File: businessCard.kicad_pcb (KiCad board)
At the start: 2 copper layers, 88.6 x 50.6 mm, 24 parts

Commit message: Perf board bottom right
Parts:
- removed the 0402 at (131.5, 55.0)
- removed the 0402 at (127.0, 49.0)
- removed the 0402 at (127.0, 55.0)
- removed the 0402 at (127.0, 52.0)
- removed the 0402 at (131.5, 52.0)
- removed the 0402 at (131.5, 49.0)
- removed the 0603 at (119.2, 58.5)
- removed the 0603 at (123.7, 65.5)
- removed the 0603 at (119.2, 65.5)
- removed the 0603 at (119.2, 62.0)
- removed the 0603 at (123.7, 62.0)
- removed the 0603 at (123.7, 58.5)
- added 0402: R_0402_1005Metric, Resistor_SMD:R_0402_1005Metric, B.Cu at (113.2, 44.0)
- added 0402: R_0402_1005Metric, Resistor_SMD:R_0402_1005Metric, B.Cu at (113.2, 50.0)
- added 0402: R_0402_1005Metric, Resistor_SMD:R_0402_1005Metric, B.Cu at (113.2, 47.0)
- added 0402: R_0402_1005Metric, Resistor_SMD:R_0402_1005Metric, B.Cu at (117.8, 47.0)
- added 0402: R_0402_1005Metric, Resistor_SMD:R_0402_1005Metric, B.Cu at (117.8, 50.0)
- added 0402: R_0402_1005Metric, Resistor_SMD:R_0402_1005Metric, B.Cu at (117.8, 44.0)
- added 0603: R_0603_1608Metric, Resistor_SMD:R_0603_1608Metric, B.Cu at (108.8, 45.0)
- added 0603: R_0603_1608Metric, Resistor_SMD:R_0603_1608Metric, B.Cu at (108.8, 52.0)
- added 0603: R_0603_1608Metric, Resistor_SMD:R_0603_1608Metric, B.Cu at (104.2, 45.0)
- added 0603: R_0603_1608Metric, Resistor_SMD:R_0603_1608Metric, B.Cu at (108.8, 48.5)
- added 0603: R_0603_1608Metric, Resistor_SMD:R_0603_1608Metric, B.Cu at (104.2, 52.0)
- added 0603: R_0603_1608Metric, Resistor_SMD:R_0603_1608Metric, B.Cu at (104.2, 48.5)
- added G***: LOGO, LOGO, B.Cu at (174.0, 57.5)
- added QFN-48-7x7mm: QFN-48-1EP_7x7mm_P0.5mm_EP3.5x3.5mm, Package_DFN_QFN:QFN-48-1EP_7x7mm_P0.5mm_EP3.5x3.5mm, B.Cu at (127.0, 72.8)
- added REF**: Perf_Board, Connector_PinHeader_2.54mm:Perf_Board, F.Cu at (184.9, 74.9)
- added Ruler: Metric_Ruler_90mm, Ruler:Metric_Ruler_98mm, B.Cu at (178.5, 86.5)
- added SOT-223: SOT-223, Package_TO_SOT_SMD:SOT-223, B.Cu at (138.5, 50.5)
- added SOT-23: SOT-23, Package_TO_SOT_SMD:SOT-23, B.Cu at (138.4, 44.5)
- added TQFP-32-7x7mm: TQFP-32_7x7mm_P0.8mm, Package_QFP:TQFP-32_7x7mm_P0.8mm, B.Cu at (127.0, 48.0)
- added TQFP-48-7x7mm: TQFP-48_7x7mm_P0.5mm, Package_QFP:TQFP-48_7x7mm_P0.5mm, B.Cu at (127.0, 61.2)
- moved 0201 15.0 mm to (104.3, 61.0)
- moved 0201 15.0 mm to (104.3, 55.0)
- moved 0201 15.0 mm to (108.8, 58.0)
- moved 0201 15.0 mm to (108.8, 55.0)
- moved 0201 15.0 mm to (108.9, 61.0)
- moved 0201 15.0 mm to (104.3, 58.0)
- moved 0805 3.96 mm to (113.2, 57.5)
- moved 0805 3.96 mm to (117.7, 53.5)
- moved 0805 3.96 mm to (117.7, 61.5)
- moved 0805 3.96 mm to (117.7, 57.5)
- moved 0805 3.96 mm to (113.2, 53.5)
- moved 0805 3.96 mm to (113.2, 61.5)
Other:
- board text added: "Linktree: linktr.ee/charlienicholson GitHub: github.com/crnicholson"
- board text added: "Mini perf board"
- board text added: "Scan for website:"
- board text added: "mm"

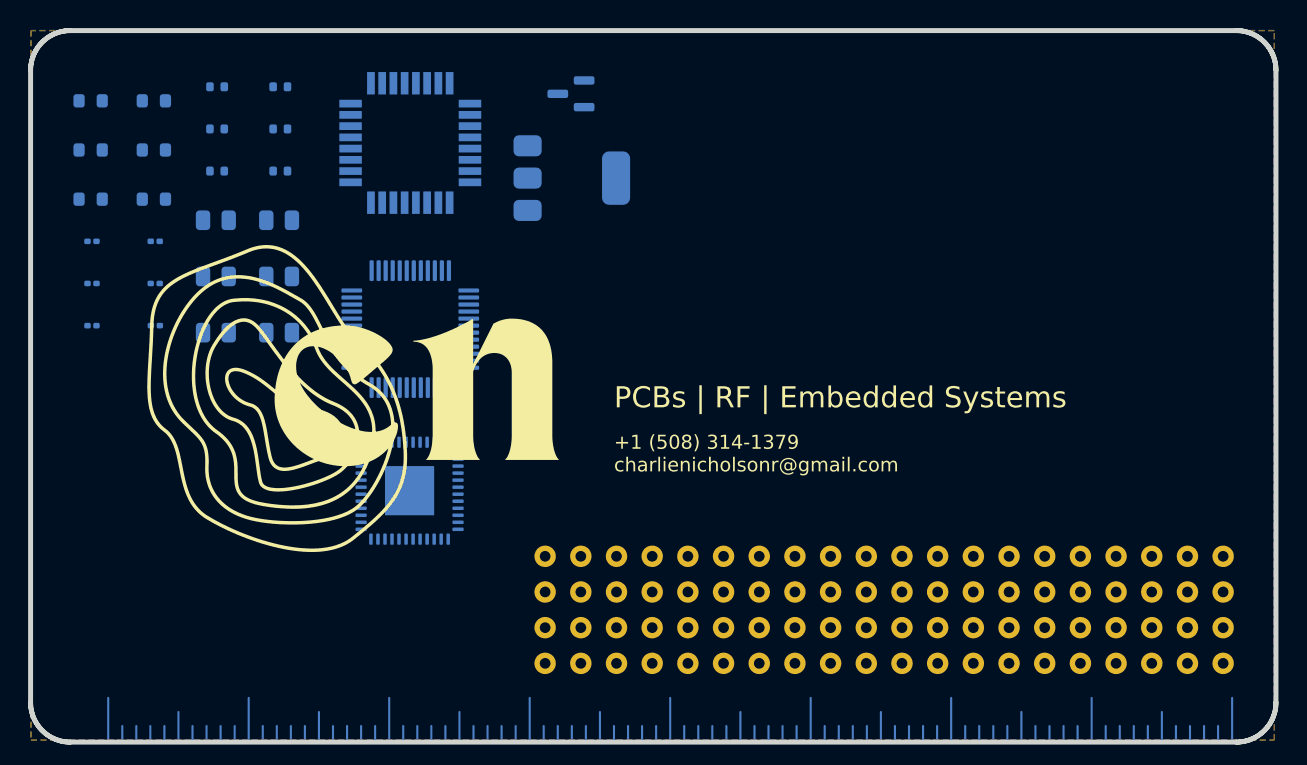
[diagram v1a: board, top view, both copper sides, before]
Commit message: Perf board on top and bottom
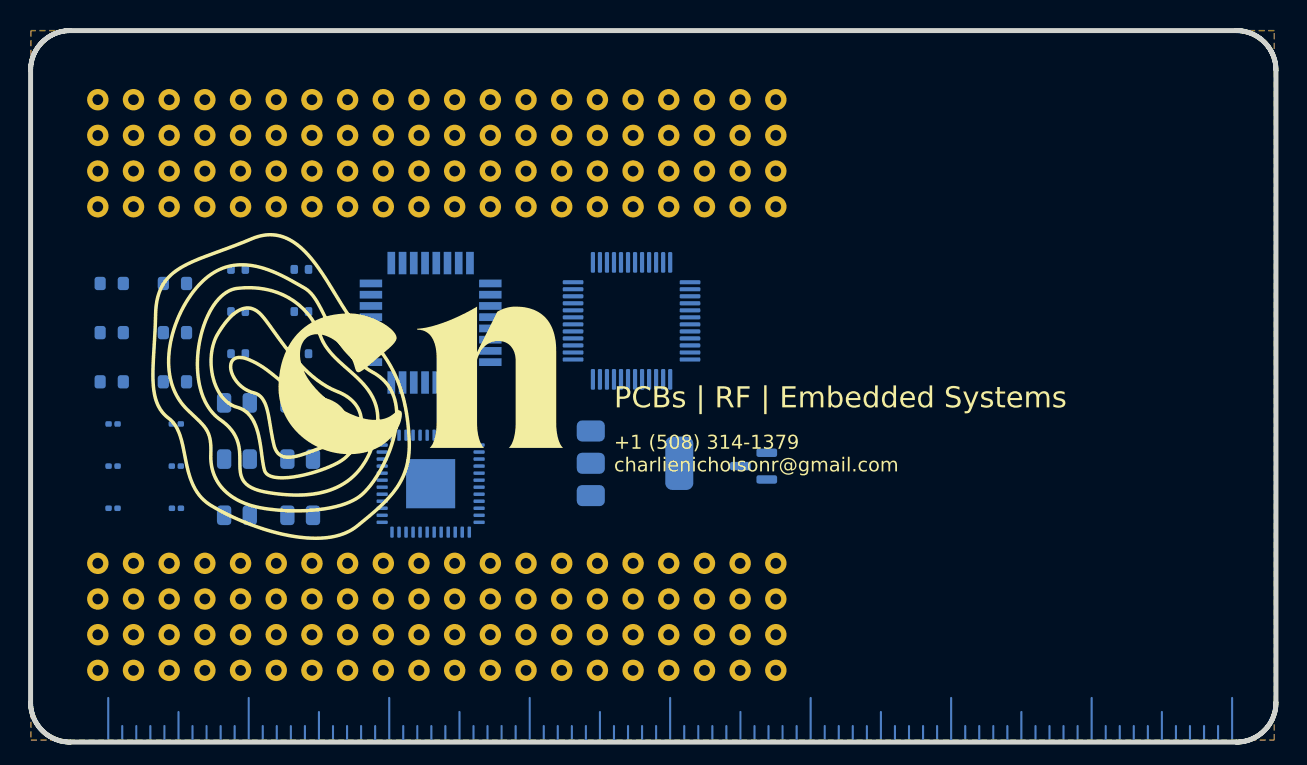
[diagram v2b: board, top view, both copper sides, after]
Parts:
- added REF**: Perf_Board, Connector_PinHeader_2.54mm:Perf_Board, F.Cu at (153.0, 42.4)
- moved REF** 31.8 mm to (153.0, 75.4)
- moved SOT-23 29.5 mm to (151.4, 71.0)
- moved SOT-223 20.8 mm to (143.0, 70.8)
- moved TQFP-48-7x7mm 15.8 mm to (142.8, 60.7)
- moved 0201 13.1 mm to (105.8, 74.0)
- moved 0201 13.1 mm to (105.8, 68.0)
- moved 0201 13.1 mm to (110.3, 71.0)
- moved 0201 13.1 mm to (110.3, 68.0)
- moved 0201 13.1 mm to (110.4, 74.0)
- moved 0201 13.1 mm to (105.8, 71.0)
- moved 0402 13.1 mm to (114.8, 57.0)
- moved 0402 13.1 mm to (114.8, 63.0)
- moved 0402 13.1 mm to (114.8, 60.0)
- moved 0402 13.1 mm to (119.2, 60.0)
- moved 0402 13.1 mm to (119.2, 63.0)
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
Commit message: Added some stuff
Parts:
- removed REF** (x2): Perf_Board, Connector_PinHeader_2.54mm:Perf_Board
- added SC-59: SC-59, Package_TO_SOT_SMD:SC-59, B.Cu at (147.8, 78.7)
- moved SOT-23 13.5 mm to (147.9, 84.0)
- moved SOT-223 10.5 mm to (139.0, 80.5)
- moved 0201 9.43 mm to (109.0, 83.3)
- moved 0201 9.43 mm to (104.5, 83.3)
- moved 0201 9.43 mm to (104.5, 77.3)
- moved 0201 9.43 mm to (109.0, 80.3)
- moved 0201 9.43 mm to (109.0, 77.3)
- moved 0201 9.43 mm to (104.5, 80.3)
- moved 0402 9.43 mm to (113.4, 66.3)
- moved 0402 9.43 mm to (113.4, 72.3)
- moved 0402 9.43 mm to (113.4, 69.3)
- moved 0402 9.43 mm to (117.9, 69.3)
- moved 0402 9.43 mm to (117.9, 72.3)
- moved 0402 9.43 mm to (117.9, 66.3)
- moved 0603 9.43 mm to (108.9, 67.3)
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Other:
- board text added: "Calculations: V_{drop} = IR P_{loss} = RI^{2}"
- board text added: "Conversions: 1 in = 25.4 mm 1 mm = 0.04 in 1 kg = 2.205 lbs 1 lb = 453.59 g Fahrenheit = (9/5 X deg C) + 32 Celsius = 5/9 X (deg F - 32)"
- board text removed: "Mini perf board"

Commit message: So close to being finished
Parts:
- added 2.5x2: , CRYSTAL-SMD-2.5X2, B.Cu at (151.5, 72.5)
- added 3.2x2.5: , CRYSTAL-SMD-3.2X2.5, B.Cu at (151.5, 66.5)
- added 5x3.2: , CRYSTAL-SMD-5X3.2, B.Cu at (158.5, 66.8)
- added BGA-121-9x9mm: BGA-121_9.0x9.0mm_Layout11x11_P0.8mm_Ball0.4mm_Pad0.35mm_NS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, Package_BGA:BGA-121_9.0x9.0mm_Layout11x11_P0.8mm_Ball0.4mm_Pad0.35mm_NSMD, B.Cu at (154.9, 58.7)
- added DFN-10: DFN-10-1EP_2.6x2.6mm_P0.5mm_EP1.3x2.2mm, Package_DFN_QFN:DFN-10-1EP_2.6x2.6mm_P0.5mm_EP1.3x2.2mm, B.Cu at (153.8, 84.5)
- added E$41: , MICROMELF-R, B.Cu at (145.2, 60.5)
- added E$42: , SC79_INFINEON, B.Cu at (146.7, 60.9)
- added E$43: , SMA-DIODE, B.Cu at (135.4, 58.9)
- added E$44: , SMB-DIODE, B.Cu at (131.5, 58.3)
- added E$47: , SOD-128, B.Cu at (138.6, 58.8)
- added E$48: , SOD-323, B.Cu at (143.4, 60.3)
- added E$49: , SOD80C, B.Cu at (141.4, 59.3)
- added E$53: , LED-GUIDE, B.Cu at (139.5, 45.5)
- added SC-70: , SC70, B.Cu at (166.7, 85.3)
- added SO-08: SO-8_3.9x4.9mm_P1.27mm, Package_SO:SO-8_3.9x4.9mm_P1.27mm, B.Cu at (115.0, 59.0)
- added SOT-143: SOT-143, Package_TO_SOT_SMD:SOT-143, B.Cu at (161.0, 84.0)
- added SOT-886: SOT-886, Package_TO_SOT_SMD:SOT-886, B.Cu at (171.3, 82.5)
- added SOT-89: SOT-89-3, Package_TO_SOT_SMD:SOT-89-3, B.Cu at (154.0, 78.0)
- added TO-252: TO-252-3_TabPin2, Package_TO_SOT_SMD:TO-252-3_TabPin2, B.Cu at (182.0, 83.5)
- added TSOP-I-28-11.8x8mm: TSOP-I-28_11.8x8mm_P0.55mm, Package_SO:TSOP-I-28_11.8x8mm_P0.55mm, B.Cu at (153.5, 46.5)
- added TSSOP-16: TSSOP-16_4.4x3.6mm_P0.4mm, Package_SO:TSSOP-16_4.4x3.6mm_P0.4mm, B.Cu at (124.1, 59.0)
- moved G*** 3.81 mm to (175.0, 57.0)
- moved SC-59 0.68 mm to (148.0, 78.0)
- moved SOT-23 0.06 mm to (148.0, 84.0)
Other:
- board text added: "40mil"
- board text added: "50"
- board text added: "60"
- board text added: "80"
- board text added: "Font Size"
- board text added: "MicroMELF"
- board text added: "MiniMELF"
- board text added: "SC79"
- board text added: "SMA"
- board text added: "SMB"
- board text added: "SOD128"
- board text added: "SOD323"
- board text added: "SOD80"

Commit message: I think I finished!
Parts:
- added L-1812: L_1812_4532Metric_Pad1.30x3.40mm_HandSolder, Inductor_SMD:L_1812_4532Metric_Pad1.30x3.40mm_HandSolder, B.Cu at (106.5, 64.5)
- added L-6.3x6.3mm: L_6.3x6.3_H3, Inductor_SMD:L_6.3x6.3_H3, B.Cu at (106.2, 57.5)
- moved SC-70 10.2 mm to (160.2, 77.5)
- moved 0201 2.16 mm to (104.5, 85.5)
- moved 0201 2.16 mm to (104.5, 79.5)
- moved 0201 2.16 mm to (109.0, 82.5)
- moved 0201 2.16 mm to (109.0, 79.5)
- moved 0201 2.16 mm to (109.0, 85.5)
- moved 0201 2.16 mm to (104.5, 82.5)
- moved 0603 2.16 mm to (108.9, 69.5)
- moved 0603 2.16 mm to (108.9, 76.5)
- moved 0603 2.16 mm to (104.4, 69.5)
- moved 0603 2.16 mm to (108.9, 73.0)
- moved 0603 2.16 mm to (104.4, 76.5)
- moved 0603 2.16 mm to (104.4, 73.0)
- moved SOT-143 1.80 mm to (162.5, 83.0)
- moved 5x3.2 1.70 mm to (158.5, 68.5)
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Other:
- board text added: "Circuit Board Business Card v1"
- board text added: "PCBs | Programming | Embedded Systems"
- board text added: "XOs:"
- board text removed: "PCBs | RF | Embedded Systems"
- board text removed: "Scan for website:"

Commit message: commit
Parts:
- moved G*** 0.50 mm to (175.0, 57.5)
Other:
- board text added: "My website:"
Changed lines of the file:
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@@
 			(plotinvisibletext no)
 			(sketchpadsonfab no)
-			(subtractmaskfromsilk no)
+			(subtractmaskfromsilk yes)
 			(outputformat 1)
 			(mirror no)
-			(drillshape 1)
+			(drillshape 0)
 			(scaleselection 1)
-			(outputdirectory "")
+			(outputdirectory "zip/")
 		)
 	)
@@
 	(footprint "LOGO"
 		(layer "B.Cu")
-		(at 175 57 180)
+		(at 175 57.5 180)
 		(property "Reference" "G***"
 			(at 0 0 180)
@@
 	)
 	(gr_rect
-		(start 163.5 69.5)
-		(end 186.5 78)
+		(start 163.5 70)
+		(end 186.5 78.5)
 		(stroke
 			(width 0.1)
@@
 		(layer "Edge.Cuts")
 	)
+	(gr_line
+		(start 100 40)
+		(end 188.5 40)
+		(stroke
+			(width 0.1)
+			(type default)
+		)
+		(layer "User.1")
+	)
+	(gr_line
+		(start 188.5 40)
+		(end 188.5 90.5)
+		(stroke
+			(width 0.1)
+			(type default)
+		)
+		(layer "User.1")
+	)
+	(gr_line
+		(start 100 90.5)
+		(end 100 40)
+		(stroke
+			(width 0.1)
+			(type default)
+		)
+		(layer "User.1")
+	)
+	(gr_line
+		(start 188.5 90.5)
+		(end 100 90.5)
+		(stroke
+			(width 0.1)
+			(type default)
+		)
+		(layer "User.1")
+	)
 	(gr_text "XOs:\n"
 		(at 161.5 66 0)
@@
 	)
 	(gr_text "Linktree: \nlinktr.ee/charlienicholson\nGitHub: \ngithub.com/crnicholson"
-		(at 186 77 0)
+		(at 186 77.5 0)
 		(layer "B.SilkS")
 		(effects
@@
 		)
 	)
-	(gr_text "Circuit Board \nBusiness Card v1"
-		(at 186.5 44 0)
+	(gr_text "Circuit Board Business Card v1"
+		(at 186.5 42.5 0)
 		(layer "B.SilkS")
 		(effects
 			(font
-				(size 1 1)
+				(size 1 0.95)
 				(thickness 0.15)
 			)
 			(justify left bottom mirror)
+		)
+	)
+	(gr_text "My website:"
+		(at 186.5 45 0)
+		(layer "B.SilkS")
+		(effects
+			(font
+				(size 1.3 1.3)
+				(thickness 0.18)
+			)
+			(justify left bottom mirror)
